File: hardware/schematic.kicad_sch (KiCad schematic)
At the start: 12 parts, among them J1 Connector_3, J2 Connector_2, J3 Connector_1, J4 Connector_4, J5 Connector_5, J6 Connector_7, U1 ESP32-S3-DevKitC

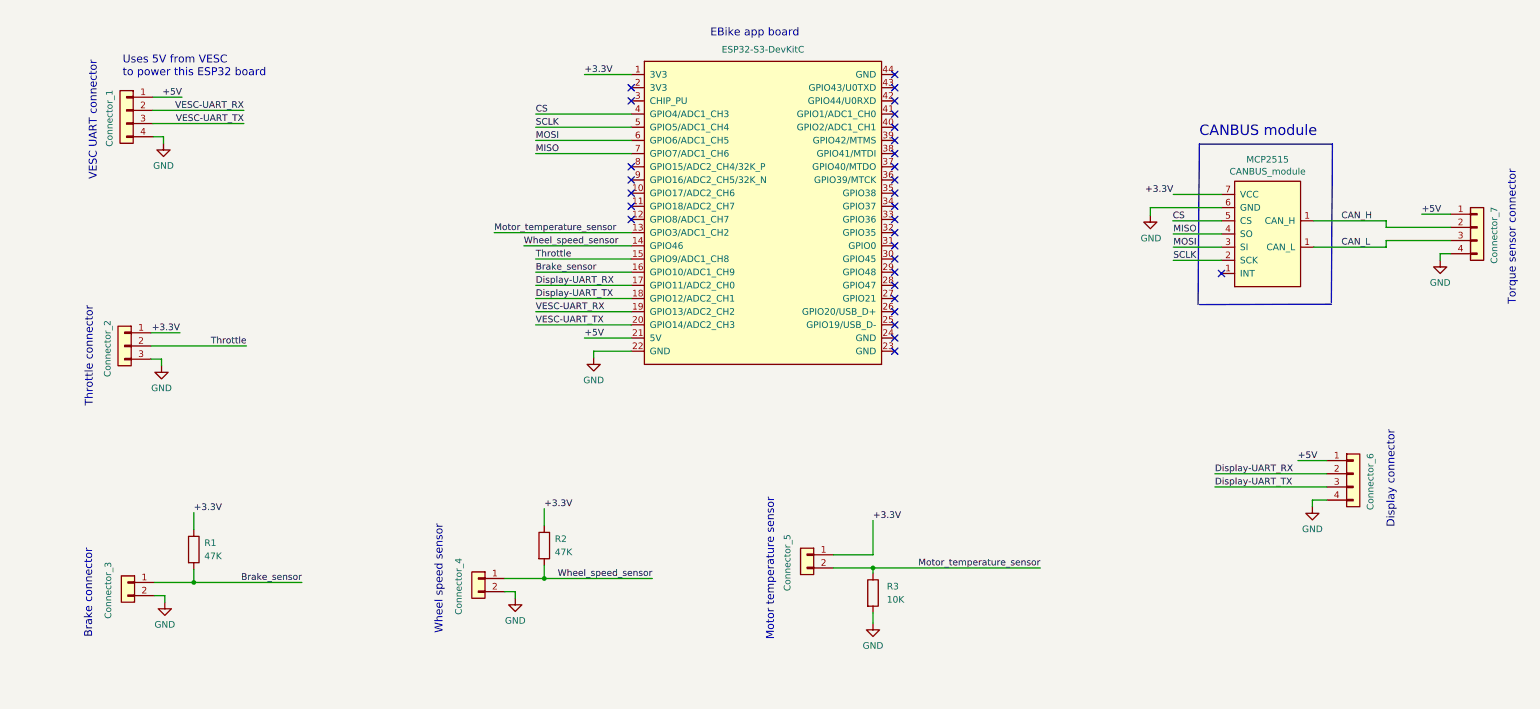
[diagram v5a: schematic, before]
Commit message: Updated schemetic with the simple CANBUS module board. Added testing firmware and pictures
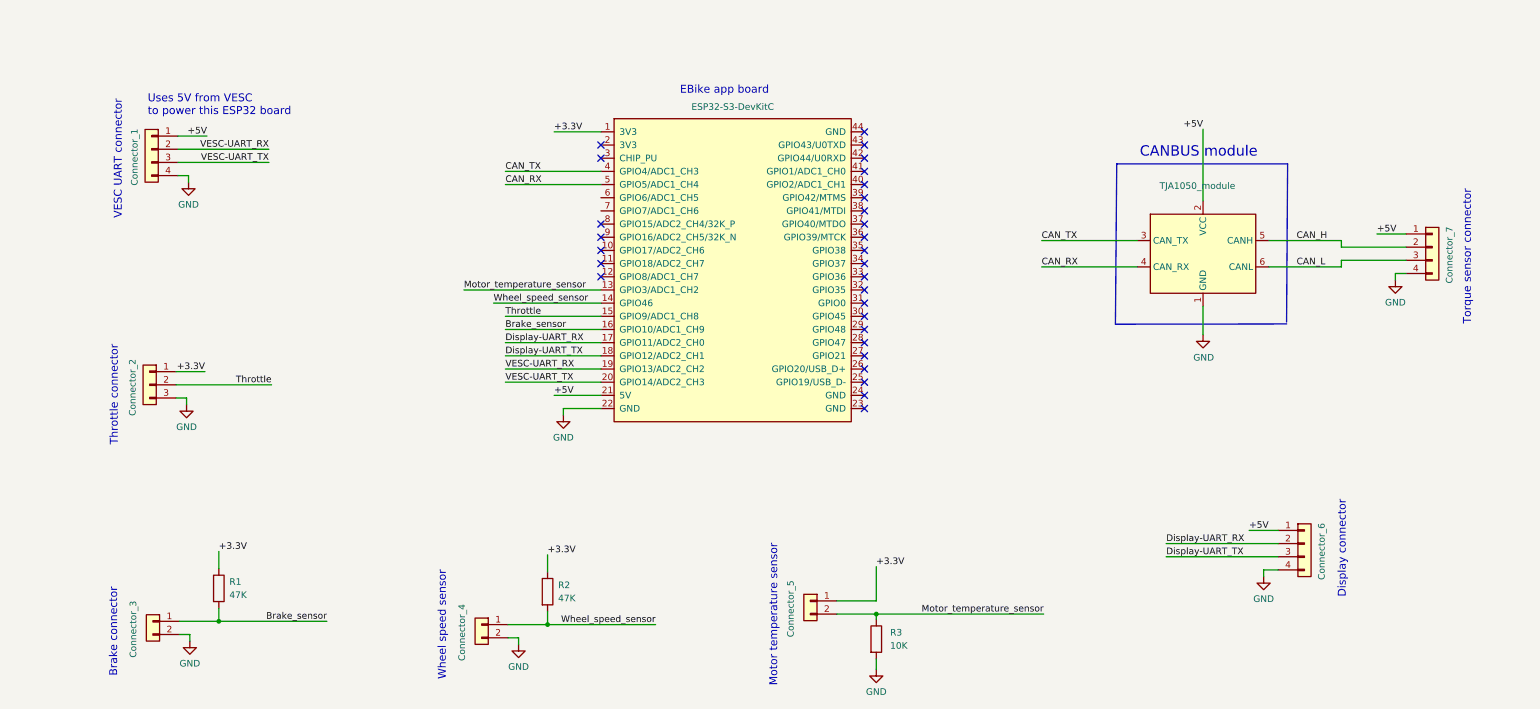
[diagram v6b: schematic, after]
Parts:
- removed MCP2515: CANBUS_module, symbol schematic-OLED_SPI-Bafang_M500_M600-rescue:CANBUS_module-canbus_module_mcp2515
- added U?: TJA1050_module, symbol TJA1050:TJA1050_module
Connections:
- net +5V: now also U?.2 (VCC)
- net CAN_H: now also U?.5 (CANH)
- net CAN_L: now also U?.6 (CANL)
- net GND: now also U?.1 (GND)
- net CS renamed CAN_TX
- net CAN_TX: now also U?.3 (CAN_TX)
- net MISO: no longer names the net of U1.7 (GPIO7/ADC1_CH6)
- net MOSI: no longer names the net of U1.6 (GPIO6/ADC1_CH5)
- net SCLK renamed CAN_RX
- net CAN_RX: now also U?.4 (CAN_RX)
- no-connect marks 30 -> 29
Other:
- moved on the sheet: R1, R2, R3

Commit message: Small changes
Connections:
- no-connect marks 29 -> 31
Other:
- note added: "TJA1050 CANBUS module"
- note removed: "CANBUS module"
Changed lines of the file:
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@@
   (junction (at 164.719 187.071) (diameter 0) (color 0 0 0 0)
   )
+  (no_connect (at 175.006 104.775))
   (no_connect (at 225.806 102.235))
   (no_connect (at 175.006 94.615))
@@
   (no_connect (at 225.806 107.315))
   (no_connect (at 225.806 109.855))
+  (no_connect (at 175.006 107.315))
   (wire (pts (xy 220.472 182.499) (xy 228.092 182.499))
     (stroke (width 0) (type default) (color 0 0 0 0))
@@
     (stroke (width 0) (type default) (color 0 0 0 0))
   )
-  (wire (pts (xy 328.168 119.38) (xy 328.168 120.65))
+  (wire (pts (xy 325.628 119.38) (xy 325.628 120.65))
     (stroke (width 0) (type default) (color 0 0 0 0))
   )
@@
     (stroke (width 0) (type default) (color 0 0 0 0))
   )
-  (wire (pts (xy 330.2 119.38) (xy 328.168 119.38))
+  (wire (pts (xy 327.66 119.38) (xy 325.628 119.38))
     (stroke (width 0) (type default) (color 0 0 0 0))
   )
@@
     (stroke (width 0) (type default) (color 0 0 0 0))
   )
-  (wire (pts (xy 317.754 116.84) (xy 330.2 116.84))
+  (wire (pts (xy 317.754 116.84) (xy 327.66 116.84))
     (stroke (width 0) (type default) (color 0 0 0 0))
   )
@@
     (stroke (width 0) (type default) (color 0 0 0 0))
   )
-  (wire (pts (xy 259.969 118.11) (xy 278.384 118.11))
+  (wire (pts (xy 262.636 118.11) (xy 278.384 118.11))
     (stroke (width 0) (type default) (color 0 0 0 0))
   )
@@
     (stroke (width 0) (type default) (color 0 0 0 0))
   )
-  (wire (pts (xy 291.084 105.41) (xy 291.084 91.567))
+  (wire (pts (xy 291.084 105.41) (xy 291.084 89.281))
     (stroke (width 0) (type default) (color 0 0 0 0))
   )
@@
     (stroke (width 0) (type default) (color 0 0 0 0))
   )
-  (wire (pts (xy 330.2 114.3) (xy 317.754 114.3))
+  (wire (pts (xy 327.66 114.3) (xy 317.754 114.3))
     (stroke (width 0) (type default) (color 0 0 0 0))
   )
@@
     (stroke (width 0) (type default) (color 0 0 0 0))
   )
-  (wire (pts (xy 330.2 111.76) (xy 324.612 111.76))
+  (wire (pts (xy 327.66 111.76) (xy 322.072 111.76))
     (stroke (width 0) (type default) (color 0 0 0 0))
   )
@@
     (stroke (width 0) (type default) (color 0 0 0 0))
   )
-  (wire (pts (xy 259.969 113.03) (xy 278.384 113.03))
+  (wire (pts (xy 262.636 113.03) (xy 278.384 113.03))
     (stroke (width 0) (type default) (color 0 0 0 0))
   )
@@
     (stroke (width 0) (type default) (color 0 0 0 0))
   )
-  (text "CANBUS module" (at 278.892 97.155 0)
-    (effects (font (size 2.0066 2.0066)) (justify left bottom))
+  (text "TJA1050\nCANBUS module" (at 281.432 96.647 0)
+    (effects (font (size 1.524 1.524)) (justify left bottom))
   )
   (text "EBike app board" (at 190.246 84.963 0)
     (effects (font (size 1.524 1.524)) (justify left bottom))
   )
-  (text "Torque sensor connector" (at 342.9 129.286 90)
+  (text "Torque sensor connector" (at 340.36 129.286 90)
     (effects (font (size 1.524 1.524)) (justify left bottom))
   )
@@
     (effects (font (size 1.27 1.27)) (justify left bottom))
   )
-  (label "+5V" (at 324.612 111.76 0)
+  (label "+5V" (at 322.072 111.76 0)
     (effects (font (size 1.27 1.27)) (justify left bottom))
   )
@@
     (effects (font (size 1.27 1.27)) (justify right bottom))
   )
-  (label "+5V" (at 291.084 91.567 180)
+  (label "+5V" (at 291.084 89.281 180)
     (effects (font (size 1.27 1.27)) (justify right bottom))
   )
@@
     (effects (font (size 1.27 1.27)) (justify left bottom))
   )
-  (label "CAN_TX" (at 259.969 113.03 0)
+  (label "CAN_TX" (at 262.636 113.03 0)
     (effects (font (size 1.27 1.27)) (justify left bottom))
   )
@@
     (effects (font (size 1.27 1.27)) (justify left bottom))
   )
-  (label "CAN_RX" (at 259.969 118.11 0)
+  (label "CAN_RX" (at 262.636 118.11 0)
     (effects (font (size 1.27 1.27)) (justify left bottom))
   )
@@
     (pin "2")
   )
-  (symbol (lib_id "Connector_Generic:Conn_01x04") (at 335.28 114.3 0) (unit 1)
-    (in_bom yes) (on_board yes)
-    (property "Reference" "J6" (id 0) (at 335.28 126.4412 0)
-      (effects (font (size 1.27 1.27)) hide)
-    )
-    (property "Value" "Connector_7" (id 1) (at 338.582 115.824 90))
-    (property "Footprint" "" (id 2) (at 335.28 114.3 0)
-      (effects (font (size 1.27 1.27)) hide)
-    )
-    (property "Datasheet" "~" (id 3) (at 335.28 114.3 0)
+  (symbol (lib_id "Connector_Generic:Conn_01x04") (at 332.74 114.3 0) (unit 1)
+    (in_bom yes) (on_board yes)
+    (property "Reference" "J6" (id 0) (at 332.74 126.4412 0)
+      (effects (font (size 1.27 1.27)) hide)
+    )
+    (property "Value" "Connector_7" (id 1) (at 336.042 115.824 90))
+    (property "Footprint" "" (id 2) (at 332.74 114.3 0)
+      (effects (font (size 1.27 1.27)) hide)
+    )
+    (property "Datasheet" "~" (id 3) (at 332.74 114.3 0)
       (effects (font (size 1.27 1.27)) hide)
     )
@@
     (pin "2")
   )
-  (symbol (lib_id "power:GND") (at 328.168 120.65 0) (mirror y) (unit 1)
-    (in_bom yes) (on_board yes)
-    (property "Reference" "#PWR09" (id 0) (at 328.168 127 0)
-      (effects (font (size 1.27 1.27)) hide)
-    )
-    (property "Value" "GND" (id 1) (at 328.168 124.968 0))
-    (property "Footprint" "" (id 2) (at 328.168 120.65 0)
-      (effects (font (size 1.27 1.27)) hide)
-    )
-    (property "Datasheet" "" (id 3) (at 328.168 120.65 0)
-      (effects (font (size 1.27 1.27)) hide)
-    )
+  (symbol (lib_id "power:GND") (at 325.628 120.65 0) (mirror y) (unit 1)
+    (in_bom yes) (on_board yes)
+    (property "Reference" "#PWR09" (id 0) (at 325.628 127 0)
+      (effects (font (size 1.27 1.27)) hide)
+    )
+    (property "Value" "GND" (id 1) (at 325.628 124.968 0))
+    (property "Footprint" "" (id 2) (at 325.628 120.65 0)
+      (effects (font (size 1.27 1.27)) hide)
+    )
+    (property "Datasheet" "" (id 3) (at 325.628 120.65 0)
+      (effects (font (size 1.27 1.27)) hide)
+    )

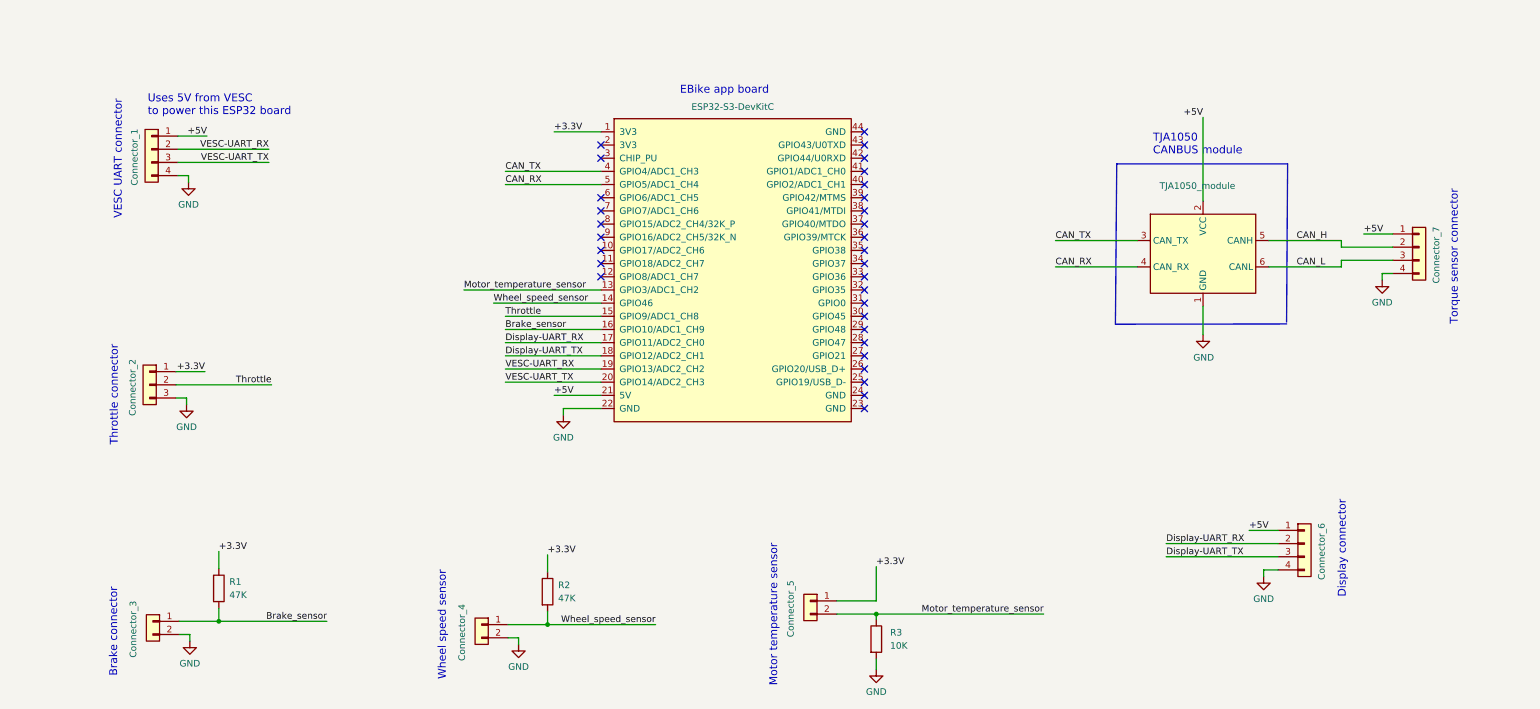
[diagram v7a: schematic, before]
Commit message: Updated the 3D file for the motor cover. Update the schematic, now equal to my final board prototype
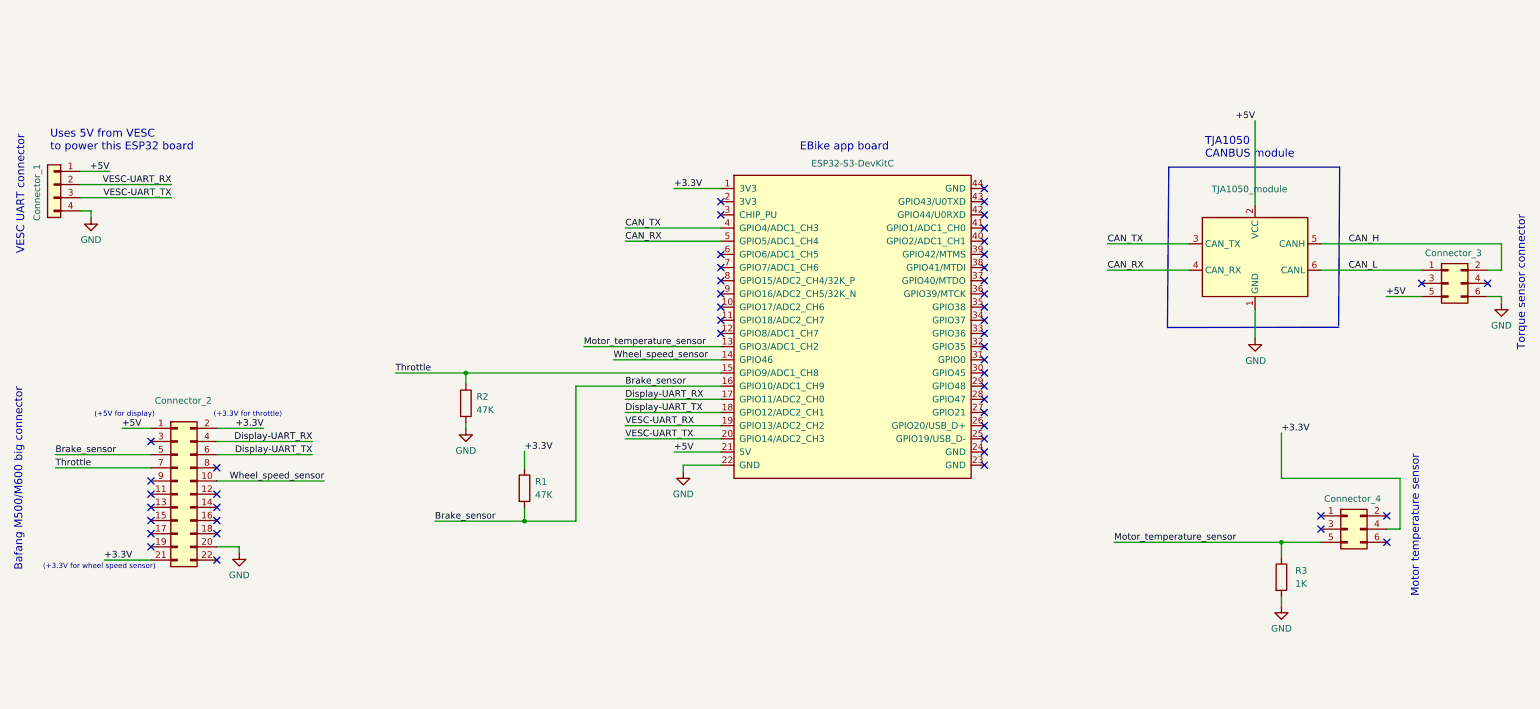
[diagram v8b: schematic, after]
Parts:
- removed J1: Connector_3, symbol Connector_Generic:Conn_01x02
- removed J2: Connector_2, symbol Connector_Generic:Conn_01x03
- removed J4: Connector_4, symbol Connector_Generic:Conn_01x02
- removed J5: Connector_5, symbol Connector_Generic:Conn_01x02
- removed J6: Connector_7, symbol Connector_Generic:Conn_01x04
- removed J?: Connector_6, symbol Connector_Generic:Conn_01x04
- added Connector_2: Conn_02x11_Odd_Even, symbol Connector_Generic:Conn_02x11_Odd_Even
- added Connector_3, Connector_4: Conn_02x03_Odd_Even, symbol Connector_Generic:Conn_02x03_Odd_Even
- R3: value 10K -> 1K
- gave numbers to parts that had none: 1
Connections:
- net +3.3V: now also Connector_2.2 (Pin_2), Connector_2.21 (Pin_21), Connector_4.4 (Pin_4); no longer R2.1
- net +5V: now also Connector_2.1 (Pin_1), Connector_3.5 (Pin_5)
- net Brake_sensor: now also Connector_2.5 (Pin_5)
- net CAN_H: now also Connector_3.2 (Pin_2)
- net CAN_L: now also Connector_3.1 (Pin_1)
- net Display-UART_RX: now also Connector_2.4 (Pin_4)
- net Display-UART_TX: now also Connector_2.6 (Pin_6)
- net GND: now also R2.2, Connector_2.20 (Pin_20), Connector_3.6 (Pin_6)
- net Motor_temperature_sensor: now also Connector_4.5 (Pin_5)
- net Throttle: now also R2.1, Connector_2.7 (Pin_7)
- net Wheel_speed_sensor: now also Connector_2.10 (Pin_10); no longer R2.2
- no-connect marks 31 -> 50
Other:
- note added: "(+3.3V for throttle)"
- note added: "(+3.3V for wheel speed sensor)"
- note added: "(+5V for display)"
- note added: "Bafang M500/M600 big connector"
- note removed: "Brake connector"
- note removed: "Display connector"
- note removed: "Throttle connector"
- note removed: "Wheel speed sensor"
- moved on the sheet: R1, R3
